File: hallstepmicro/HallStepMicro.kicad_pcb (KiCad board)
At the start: 2 copper layers, 33 x 55.9 mm, 26 parts, among them IC1 ATTINY84A-SS

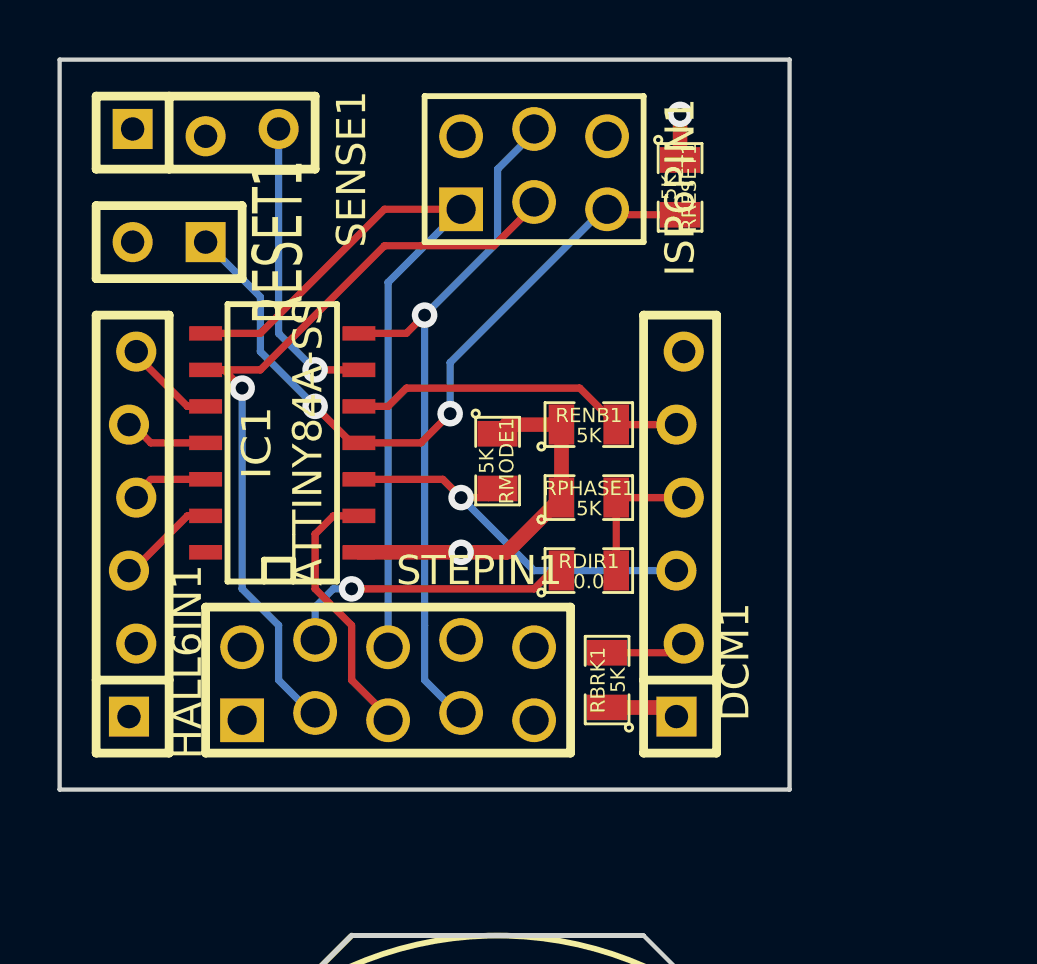
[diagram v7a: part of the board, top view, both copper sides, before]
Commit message: Adding OSHPark Minimum rule settings.
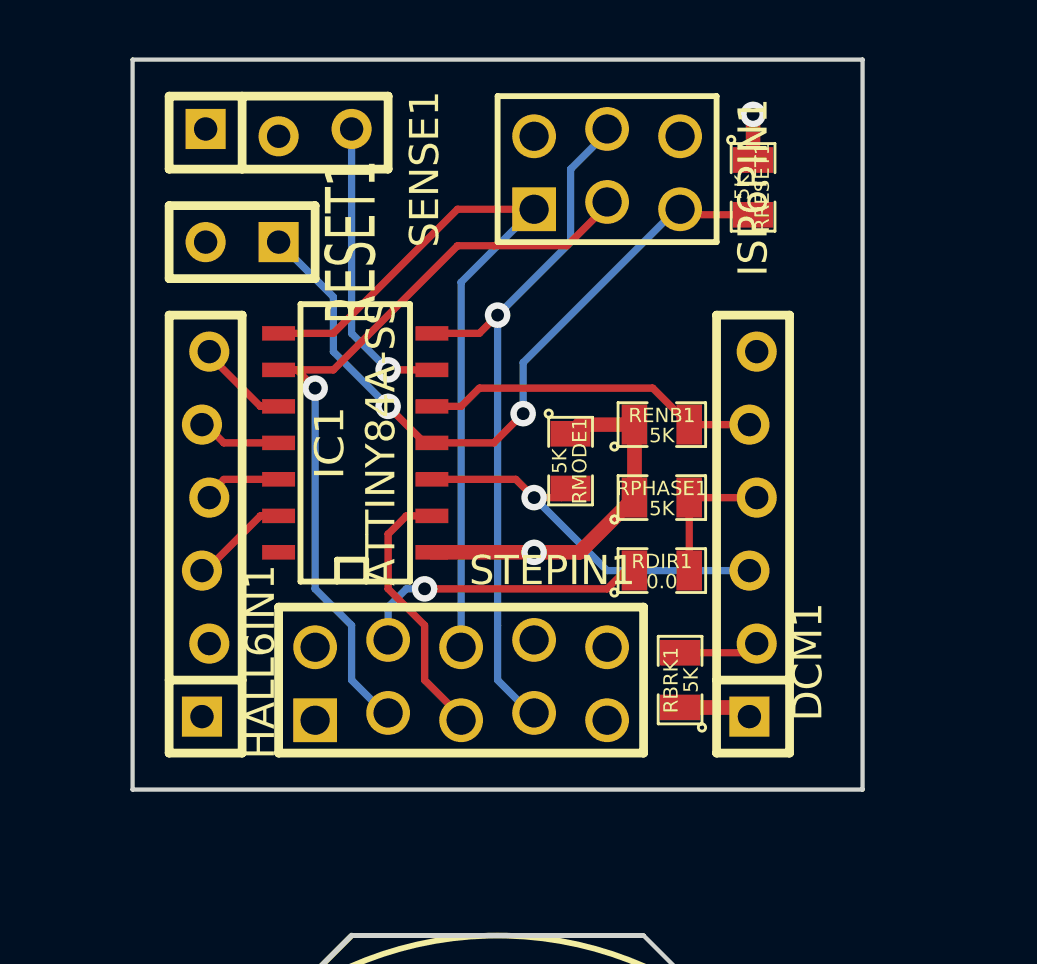
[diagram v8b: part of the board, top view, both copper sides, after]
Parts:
- moved HALL6IN1 2.54 mm to (116.8, 49.5)
- moved IC1 2.54 mm to (121.9, 46.4)
- moved RESET1 2.54 mm to (118.1, 39.4)
- moved STEPIN1 2.54 mm to (125.7, 54.6)
- moved DCM1 2.54 mm to (135.9, 49.5)
- moved ISP6PIN1 2.54 mm to (130.8, 36.8)
- moved RBRK1 2.54 mm to (133.3, 54.6)
- moved RDIR1 2.54 mm to (132.7, 50.8)
- moved RENB1 2.54 mm to (132.7, 45.7)
- moved RMODE1 2.54 mm to (129.5, 47.0)
- moved RPHASE1 2.54 mm to (132.7, 48.3)
- moved RRESET1 2.54 mm to (135.9, 37.5)
- moved SENSE1 2.54 mm to (119.4, 35.6)
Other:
- board size 33 x 55.9 mm -> 30.5 x 55.9 mm
- net class OSHPark_Minimum added: clearance 0.1524, trace_width 0.1524, via_dia 0.508, via_drill 0.3302
- rule trace_min: 0.254 -> 0.1524
- rule via_min_drill: 0.508 -> 0.3302
- rule via_min_size: 0.889 -> 0.508
